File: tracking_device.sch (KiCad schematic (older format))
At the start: 57 parts, among them J1 USB_OTG, J2 CONN_01X02, J3 CONN_01X02, J4 CONN_01X02, J5 CONN_01X02, J6 JST-PH, J7 Micro_SD_Connector, Q1 Si2343DS, U1 RClamp0503F, U2 SAM-M8, U3 MCP73831, U4 STC3100, U5 REG113NA-3.3

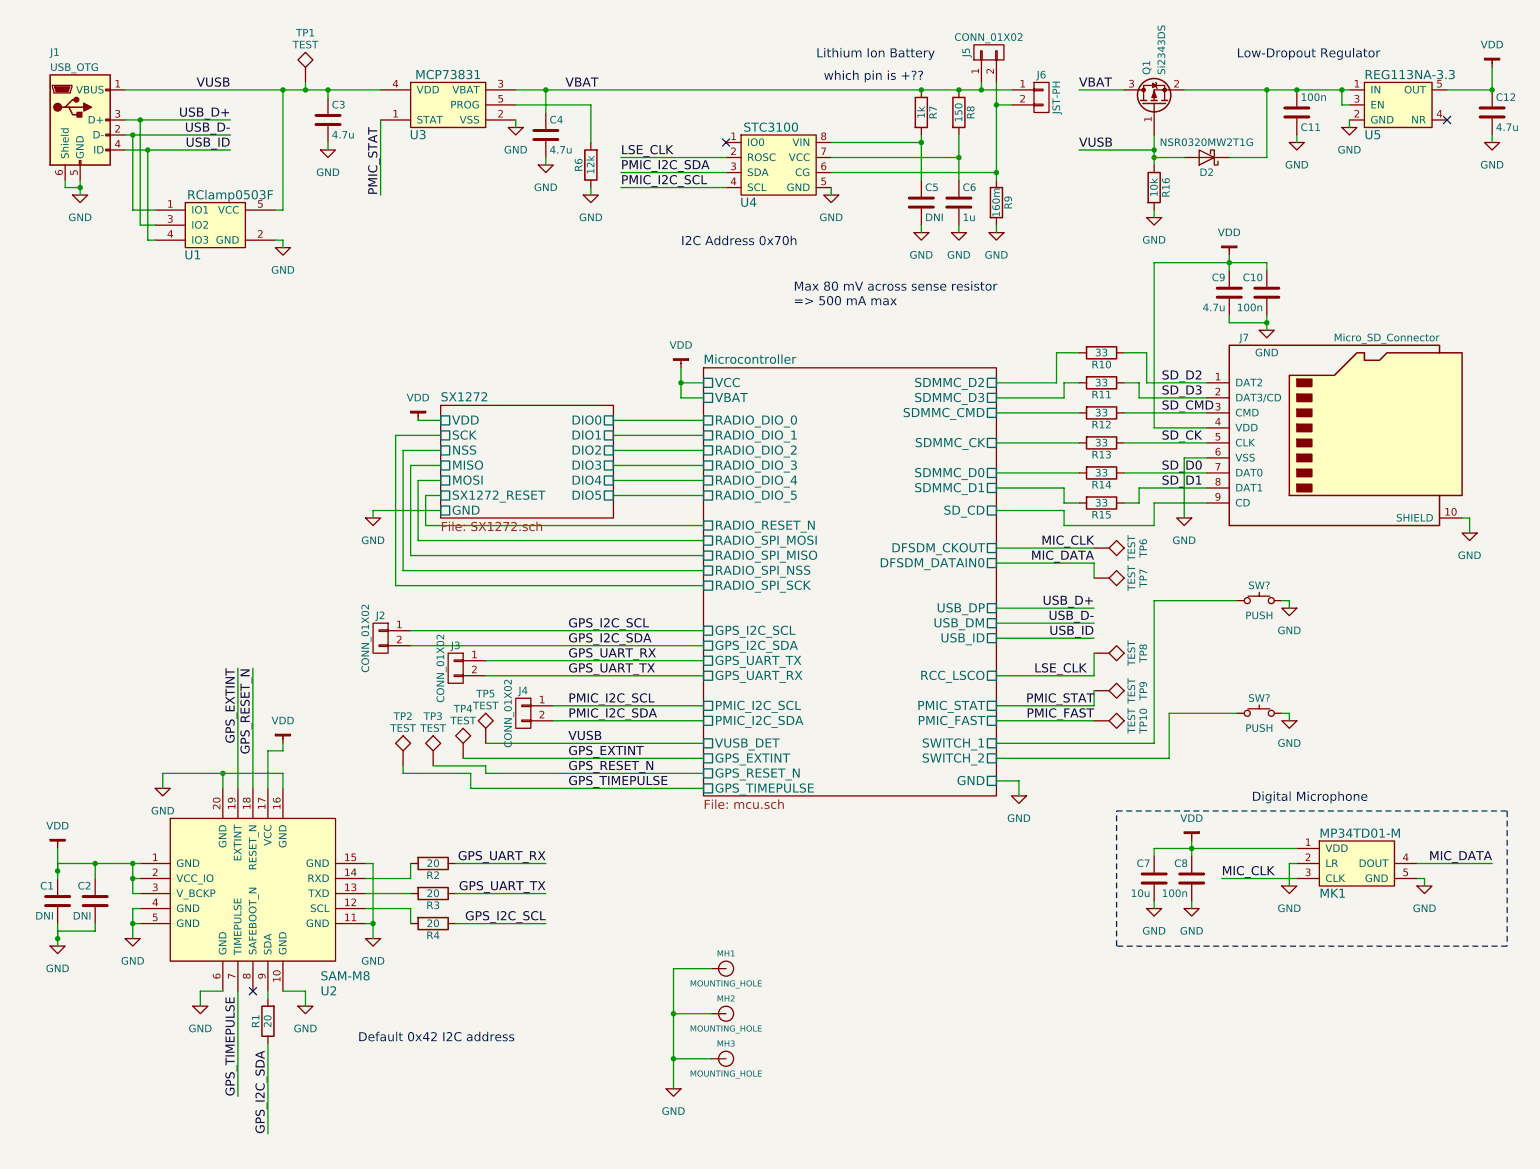
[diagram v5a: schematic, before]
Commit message: Rev 3 DRC clean
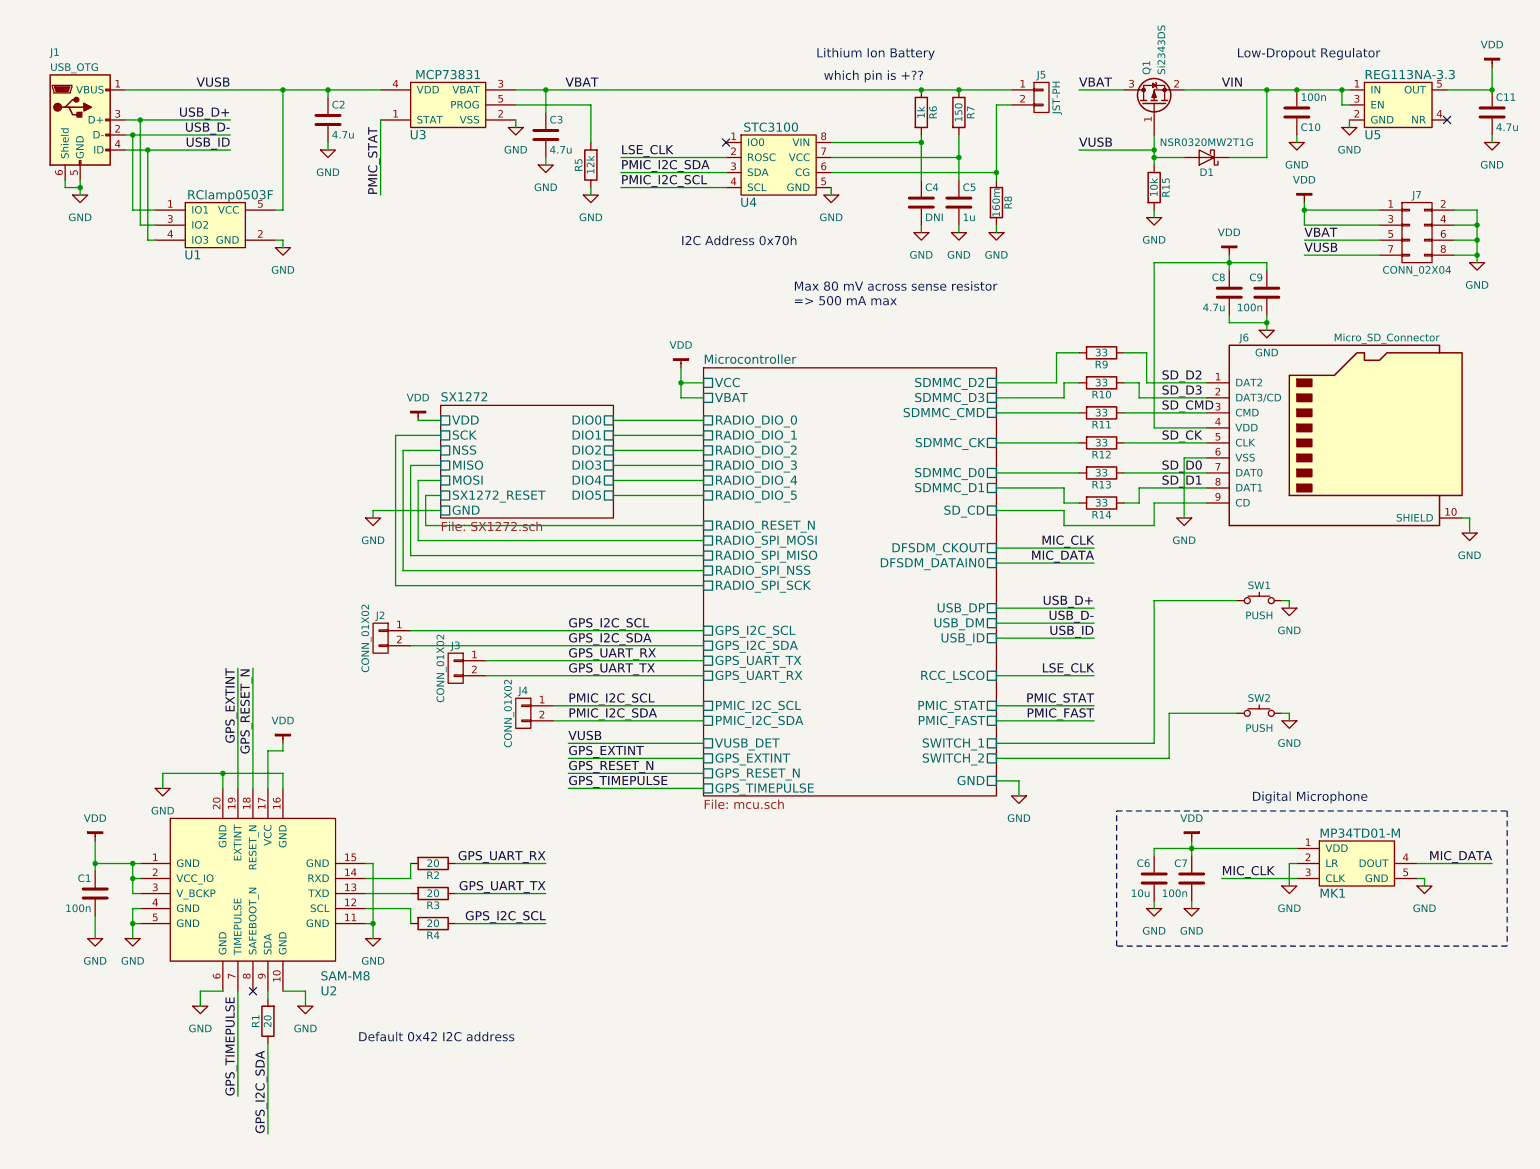
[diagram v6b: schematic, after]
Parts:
- removed C2: DNI, Capacitors_SMD:C_0805_HandSoldering, symbol C
- removed J5: CONN_01X02, tracking_device:Pin_Header_Straight_2x01_Pitch2.54mm, symbol CONN_01X02
- removed MH1, MH2, MH3: MOUNTING_HOLE, Mounting_Holes:MountingHole_2.2mm_M2, symbol MOUNTING_HOLE
- removed TP1, TP10, TP2, TP3, TP4, TP5, TP6, TP7, TP8, TP9: TEST, Measurement_Points:Measurement_Point_Round-TH_Small, symbol TEST
- added J7: CONN_02X04, tracking_device:HEADER_M_2.54MM_2R8P_ST_AU_PTH, symbol CONN_02X04
- C1: value DNI -> 100n
- SW1, SW2: renamed from SW?; footprint (none) -> tracking_device:SW_3.1x3.1; URL (none) -> https://lcsc.com/product-detail/Tactile-Switches_K2-1102SP-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
- renumbered C11 to C10, C12 to C11, C3 to C2, C4 to C3, C5 to C4, C6 to C5, C7 to C6, C8 to C7, C9 to C8, C10 to C9, D2 to D1, J6 to J5, J7 to J6, R11 to R10, R12 to R11, R13 to R12, R14 to R13, R15 to R14, R16 to R15, R6 to R5, R7 to R6, R8 to R7, R9 to R8, R10 to R9
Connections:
- net GND: now also J7.2 (P2), J7.4 (P4), J7.6 (P6), J7.8 (P8)
- net VBAT: now also J7.5 (P5)
- net VDD: now also J7.1 (P1), J7.3 (P3)
- net VUSB: now also J7.7 (P7)
- net VIN: now reaches C10.2, D1.1 (K), Q1.2 (S), U5.1 (IN), U5.3 (EN)
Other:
- moved on the sheet: C1
